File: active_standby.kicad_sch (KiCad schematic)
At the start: 22 parts, among them Q10 2N7002TQ-7-F, Q11 2N7002TQ-7-F, Q2 2N7002TQ-7-F, Q8 2N7002TQ-7-F, Q9 2N7002TQ-7-F, U24 SN3257QDYYRQ1, U30 SN3257QDYYRQ1

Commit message: Add licensing
Use CERN-OHL-W version 2

Signed-off-by: Corey Minyard <corey@minyard.net>
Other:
- company: (none) -> AMSAT-NA
- title: (none) -> Active Standby Switching Logic
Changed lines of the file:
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@@
 	(generator_version "10.0")
 	(paper "A4")
+	(title_block
+		(title "Active Standby Switching Logic")
+		(date "2026-08-20")
+		(rev "4.0")
+		(company "AMSAT-NA")
+		(comment 1 "AE5KM")
+		(comment 2 "Copyright Corey Minyard, 2026")
+		(comment 3 "Licensed under CERN-OHL-W version 2")
+	)
 	(text "Remove for board 1\nPopulate for board 2"
 		(exclude_from_sim no)

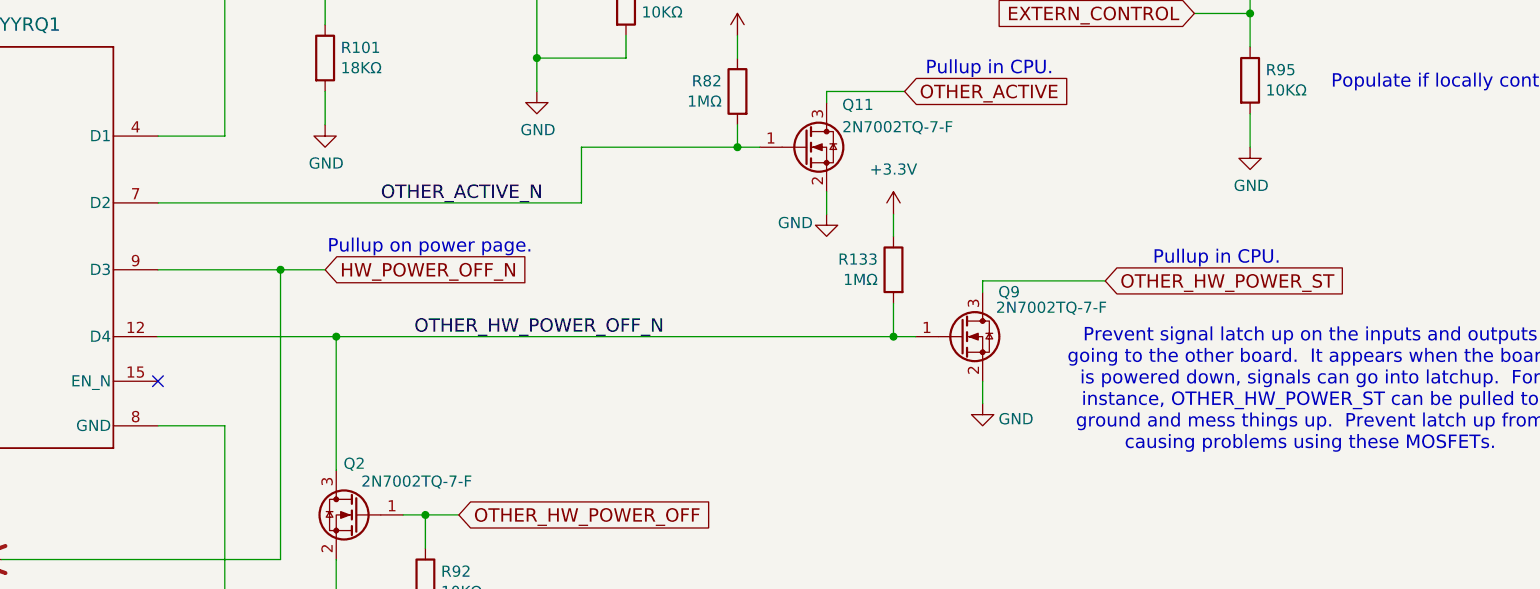
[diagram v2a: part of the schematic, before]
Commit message: Change C125 to .6pF
That has a better notch at 1340MHz.

Signed-off-by: Corey Minyard <corey@minyard.net>
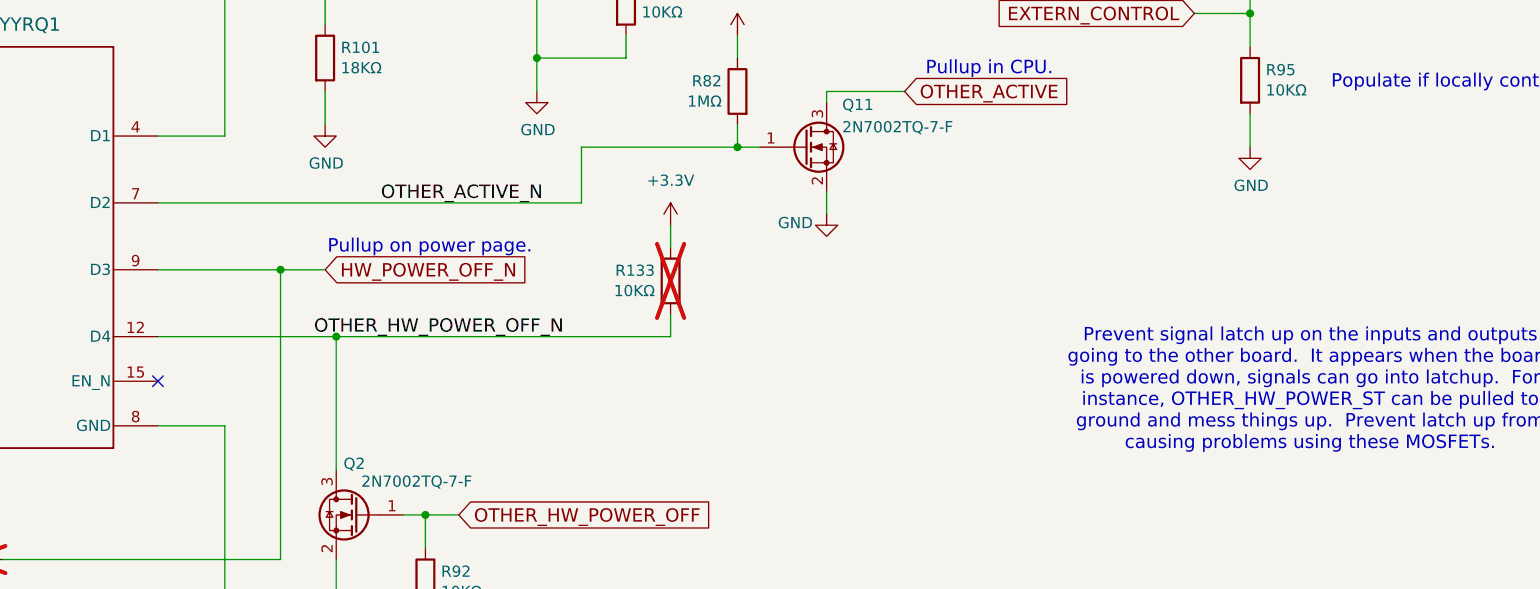
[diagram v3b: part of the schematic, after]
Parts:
- removed Q9: 2N7002TQ-7-F, Package_TO_SOT_SMD:SOT-523, symbol PACSAT_DEV_misc:2N7002TQ-7-F
- R133: value 1MΩ -> 10KΩ; now not fitted; now left out of the parts list
